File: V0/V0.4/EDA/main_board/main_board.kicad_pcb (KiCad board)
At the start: 2 copper layers, 40.6 x 78.5 mm, 29 parts, among them U1 top_rail_v2

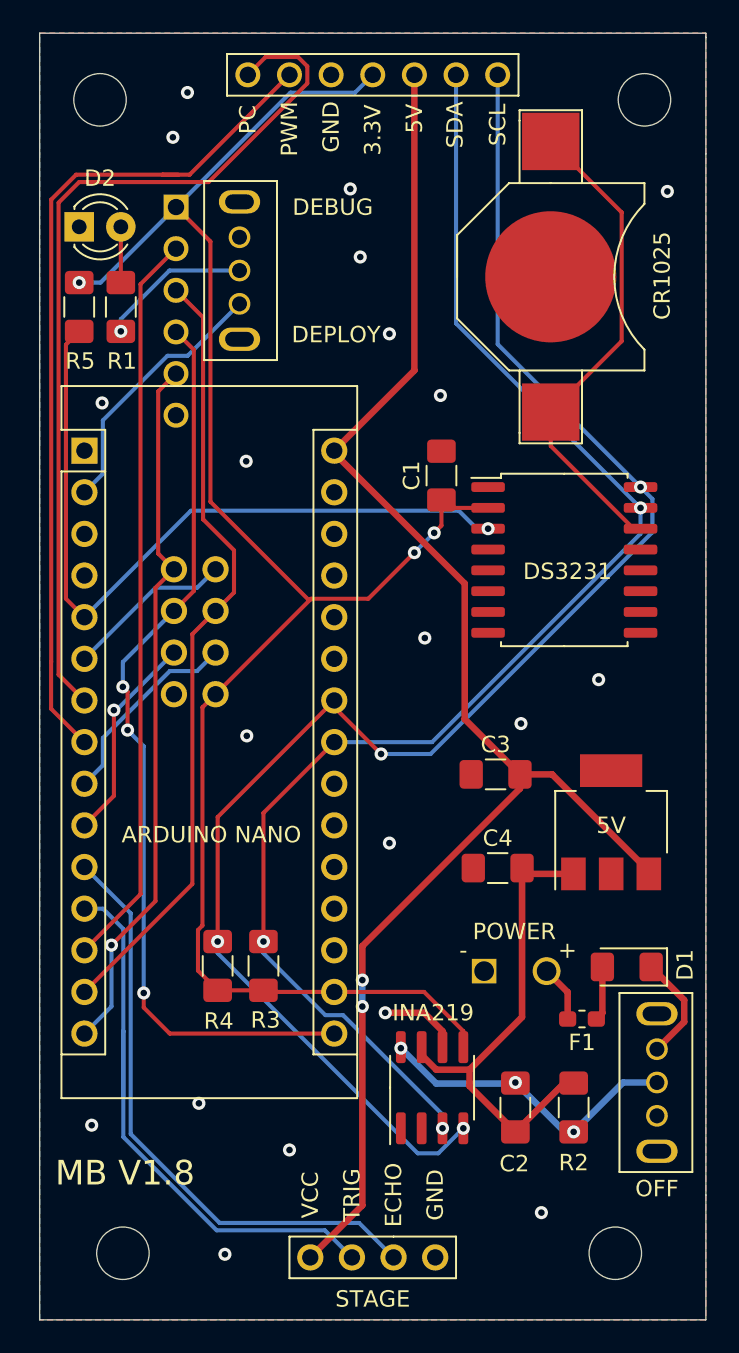
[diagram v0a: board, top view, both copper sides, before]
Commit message: update magnet_toggle.ino
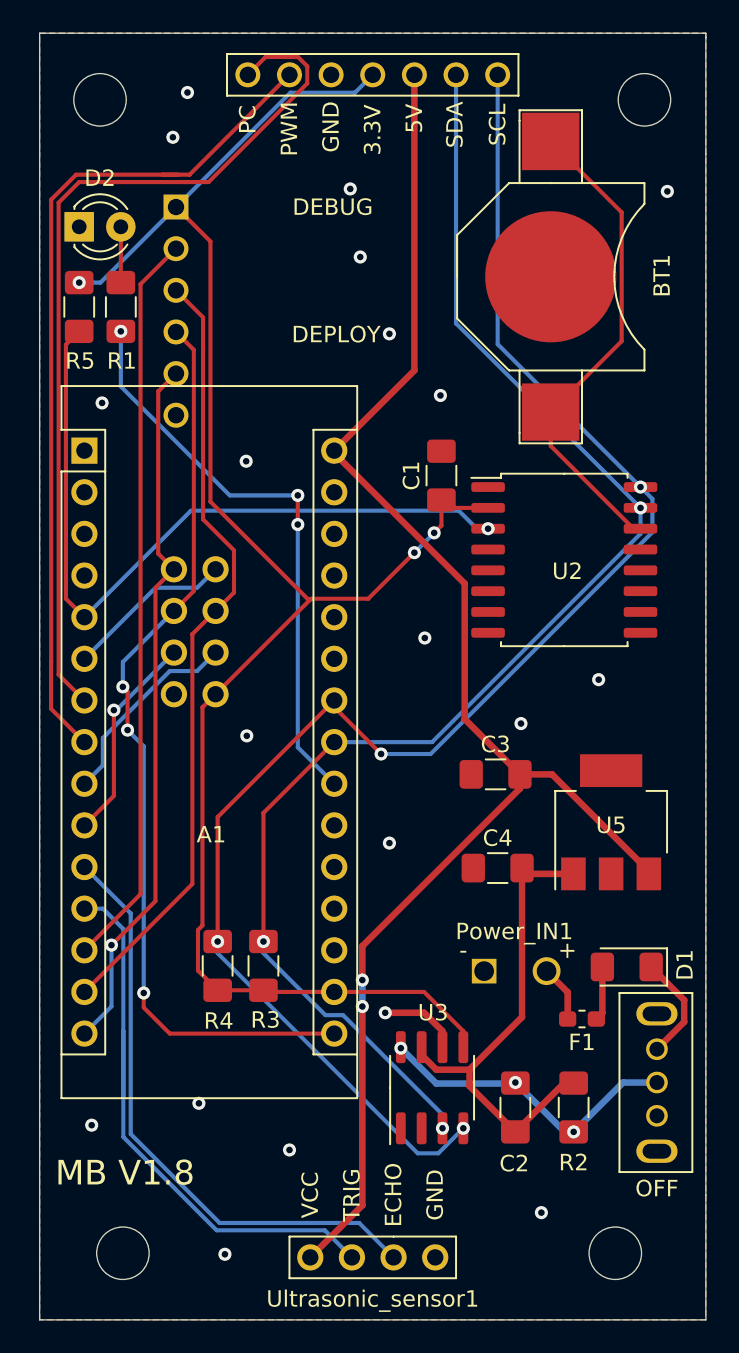
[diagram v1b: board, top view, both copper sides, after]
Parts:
- removed switch2: grounded_switch, ARTS-Lab:grounded_switch
- A1: renamed from ARDUINO NANO
- Micro_SD1: renamed from MICRO SD
- renumbered CR1025 to BT1, POWER to Power_IN1, DS3231 to U2, INA219 to U3, 5V to U5, STAGE to Ultrasonic_sensor1
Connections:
- R1 pad 1: Net-(R1-Pad1) -> Net-(A1-Pad22)
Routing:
- net Net-(A1-Pad22): track 0.00 -> 35.4 mm, vias 0 -> 3
- net Net-(A1-Pad2): track 16.1 -> 0.00 mm
- net Net-(R1-Pad1): track 9.21 -> 0.00 mm, vias 1 -> 0
